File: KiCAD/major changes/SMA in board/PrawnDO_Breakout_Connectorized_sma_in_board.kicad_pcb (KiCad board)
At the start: 2 copper layers, 113 x 86.8 mm, 83 parts, among them IC1 74LVT245D,118, IC2 74LVT245D,118, IC3 74LVT245D,118, IC4 74LVT245D,118, J1 do15, J10 do6, J11 do5, J12 do4, J13 do3, J14 do2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

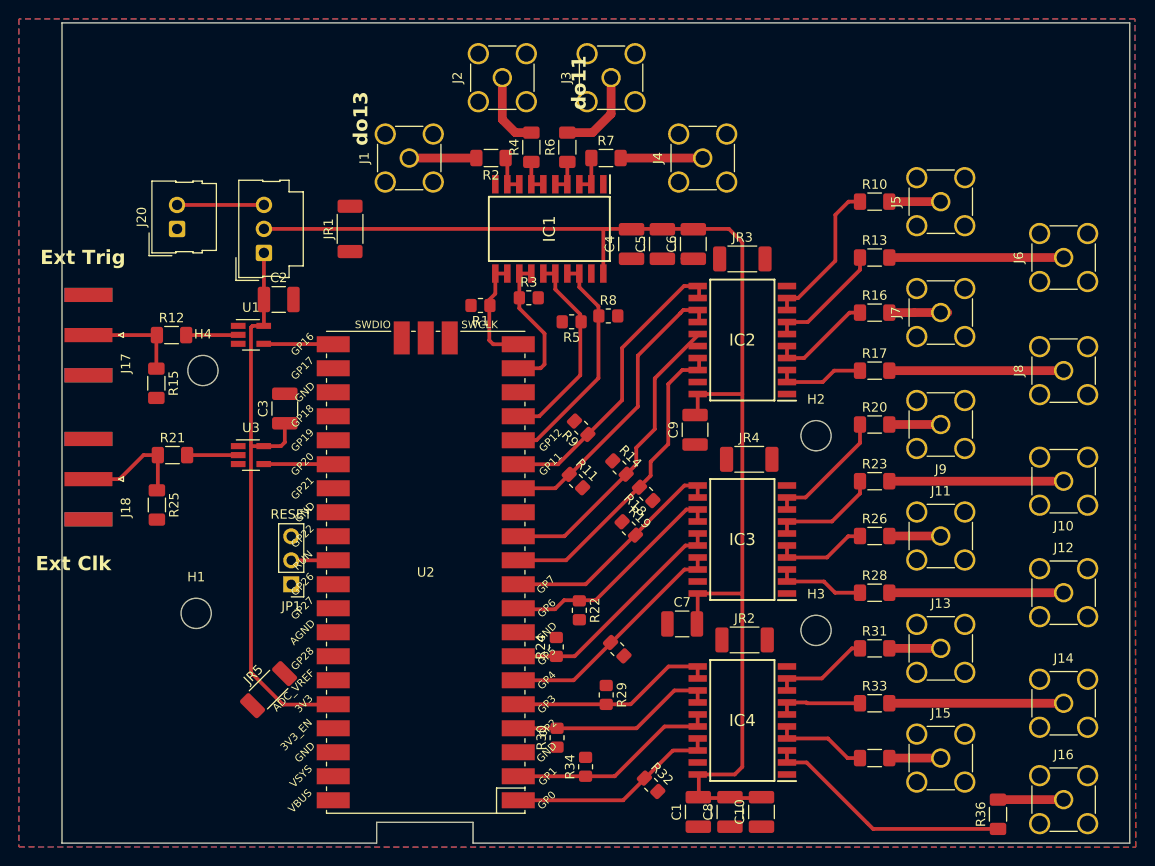
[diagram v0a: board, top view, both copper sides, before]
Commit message: Trace changes
Fixed some traces and added a connection to ground through pins on pico

Also made slot for USB slightly larger.

Moved resistor on bottom of board

Changed header footprint
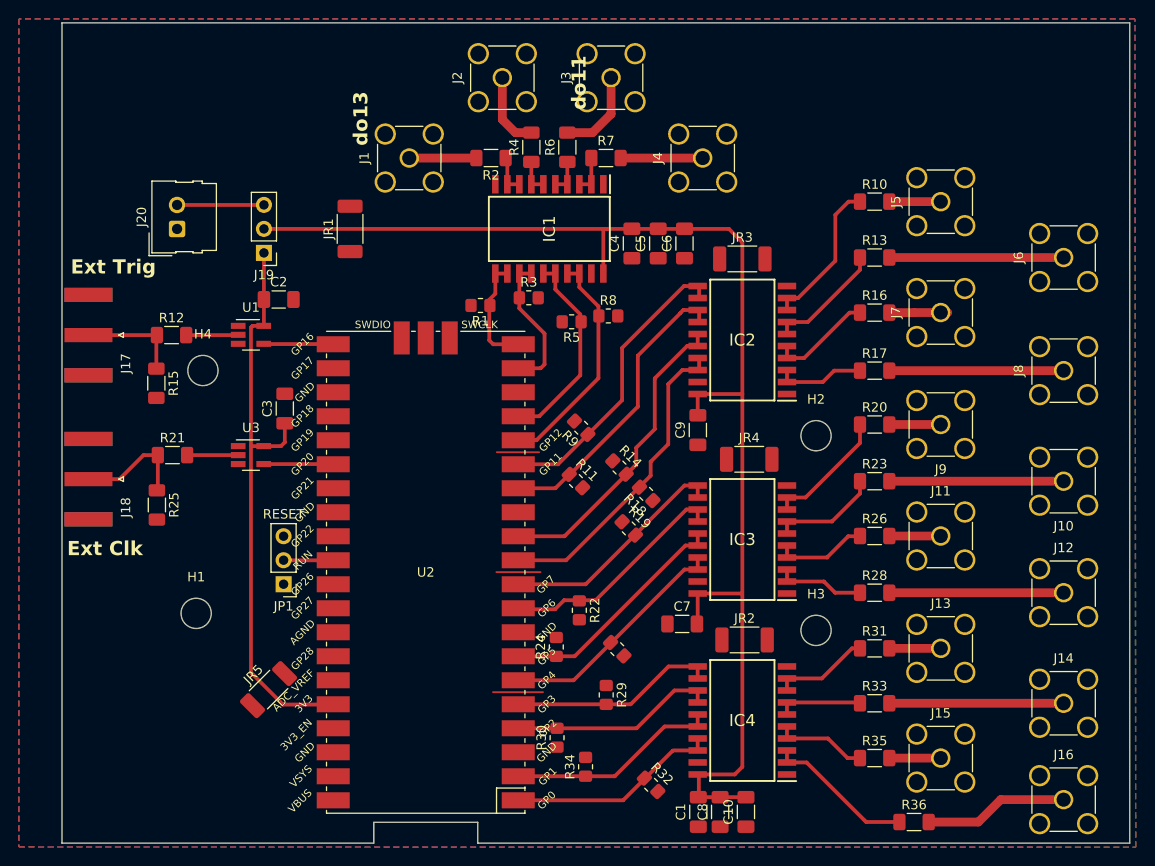
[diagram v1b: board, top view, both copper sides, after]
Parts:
- C1, C10, C2, C3, C4, C5, C6, C7, C8, C9: footprint Capacitor_SMD:C_1210_3225Metric_Pad1.33x2.70mm_HandSolder -> Capacitor_SMD:C_1206_3216Metric_Pad1.33x1.80mm_HandSolder
- J19: value Conn_01x03 -> PWR SEL; footprint Connector_Molex:Molex_SL_171971-0003_1x03_P2.54mm_Vertical -> Connector_PinHeader_2.54mm:PinHeader_1x03_P2.54mm_Vertical
- J20: value Conn_01x02 -> EXT PWR
- moved R36 8.92 mm to (162.1, 138.8), turned to 0 degrees
- moved C10 1.64 mm to (144.3, 137.7)
- moved C8 1.04 mm to (141.5, 137.7)
- moved C6 0.94 mm to (137.8, 77.5)
- moved JP1 0.81 mm to (95.3, 113.6)
- moved C5 0.44 mm to (135.0, 77.5)
- moved C9 0.30 mm to (139.2, 97.3)
- moved C4 0.07 mm to (132.2, 77.5)
- turned J19 to 180 degrees
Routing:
- net GND: track 0.00 -> 14.4 mm
- net Net-(IC4A-A0): track 26.5 -> 15.8 mm
- net do0: track 6.94 -> 15.3 mm
- net Power  Supply: track 140.3 -> 138.8 mm
- net Net-(JP1-C): track 5.36 -> 6.17 mm
- net Net-(IC2A-B2): track 33.1 -> 33.7 mm
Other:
- outline, holes or cut-outs redrawn

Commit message: Moved around mounting holes
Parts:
- moved H4 3.49 mm to (86.7, 94.5)
- moved H1 3.22 mm to (86.7, 113.5)
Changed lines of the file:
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@@
   )
   (footprint "MountingHole:MountingHole_3.2mm_M3_ISO7380" (layer "F.Cu")
-    (at 86.817 90.986)
+    (at 86.699896 94.475)
     (descr "Mounting Hole 3.2mm, no annular, M3, ISO7380")
     (tags "mounting hole 3.2mm no annular m3 iso7380")
@@
     (property "ki_keywords" "R res resistor")
     (attr smd)
-    (fp_text reference "R25" (at 0 -1.82 -90) (layer "F.SilkS")
+    (fp_text reference "R25" (at 0 -1.82 90) (layer "F.SilkS")
         (effects (font (size 1 1) (thickness 0.15)))
     )
-    (fp_text value "47k" (at 0 1.82 -90) (layer "F.Fab")
+    (fp_text value "47k" (at 0 1.82 90) (layer "F.Fab")
         (effects (font (size 1 1) (thickness 0.15)))
     )
-    (fp_text user "${REFERENCE}" (at 0 0 -90) (layer "F.Fab")
+    (fp_text user "${REFERENCE}" (at 0 0 90) (layer "F.Fab")
         (effects (font (size 0.8 0.8) (thickness 0.12)))
     )
@@
         (effects (font (size 1 1) (thickness 0.15)))
     )
-    (fp_text value "EXT PWR" (at 6.217 0.876 180) (layer "F.Fab")
+    (fp_text value "EXT PWR" (at 6.217 0.876) (layer "F.Fab")
         (effects (font (size 1 1) (thickness 0.15)))
     )
@@
         (effects (font (size 1 1) (thickness 0.15)))
     )
-    (fp_text user "GP0" (at -12.8 -24.13 225) (layer "F.SilkS")
+    (fp_text user "GP0" (at -12.8 -24.13 45) (layer "F.SilkS")
         (effects (font (size 0.8 0.8) (thickness 0.15)))
     )
@@
         (effects (font (size 0.8 0.8) (thickness 0.15)))
     )
-    (fp_text user "GP5" (at -12.8 -8.89 225) (layer "F.SilkS")
+    (fp_text user "GP5" (at -12.8 -8.89 45) (layer "F.SilkS")
         (effects (font (size 0.8 0.8) (thickness 0.15)))
     )
-    (fp_text user "GP1" (at -12.9 -21.6 225) (layer "F.SilkS")
+    (fp_text user "GP1" (at -12.9 -21.6 45) (layer "F.SilkS")
         (effects (font (size 0.8 0.8) (thickness 0.15)))
     )
@@
         (effects (font (size 0.8 0.8) (thickness 0.15)))
     )
-    (fp_text user "GP3" (at -12.8 -13.97 225) (layer "F.SilkS")
+    (fp_text user "GP3" (at -12.8 -13.97 45) (layer "F.SilkS")
         (effects (font (size 0.8 0.8) (thickness 0.15)))
     )
@@
         (effects (font (size 0.8 0.8) (thickness 0.15)))
     )
-    (fp_text user "GND" (at -12.8 -19.05 225) (layer "F.SilkS")
+    (fp_text user "GND" (at -12.8 -19.05 45) (layer "F.SilkS")
         (effects (font (size 0.8 0.8) (thickness 0.15)))
     )
@@
         (effects (font (size 0.8 0.8) (thickness 0.15)))
     )
-    (fp_text user "GP6" (at -12.8 -3.81 225) (layer "F.SilkS")
+    (fp_text user "GP6" (at -12.8 -3.81 45) (layer "F.SilkS")
         (effects (font (size 0.8 0.8) (thickness 0.15)))
     )
@@
         (effects (font (size 0.8 0.8) (thickness 0.15)))
     )
-    (fp_text user "GP7" (at -12.7 -1.3 225) (layer "F.SilkS")
+    (fp_text user "GP7" (at -12.7 -1.3 45) (layer "F.SilkS")
         (effects (font (size 0.8 0.8) (thickness 0.15)))
     )
@@
         (effects (font (size 0.8 0.8) (thickness 0.15)))
     )
-    (fp_text user "GP4" (at -12.8 -11.43 225) (layer "F.SilkS")
+    (fp_text user "GP4" (at -12.8 -11.43 45) (layer "F.SilkS")
         (effects (font (size 0.8 0.8) (thickness 0.15)))
     )
@@
         (effects (font (size 0.8 0.8) (thickness 0.15)))
     )
-    (fp_text user "GND" (at -12.8 -6.35 225) (layer "F.SilkS")
+    (fp_text user "GND" (at -12.8 -6.35 45) (layer "F.SilkS")
         (effects (font (size 0.8 0.8) (thickness 0.15)))
     )
-    (fp_text user "GP2" (at -12.9 -16.51 225) (layer "F.SilkS")
+    (fp_text user "GP2" (at -12.9 -16.51 45) (layer "F.SilkS")
         (effects (font (size 0.8 0.8) (thickness 0.15)))
     )
@@
     (property "ki_keywords" "R res resistor")
     (attr smd)
-    (fp_text reference "R15" (at 0 -1.82 -90) (layer "F.SilkS")
+    (fp_text reference "R15" (at 0 -1.82 90) (layer "F.SilkS")
         (effects (font (size 1 1) (thickness 0.15)))
     )
-    (fp_text value "47k" (at 0 1.82 -90) (layer "F.Fab")
+    (fp_text value "47k" (at 0 1.82 90) (layer "F.Fab")
         (effects (font (size 1 1) (thickness 0.15)))
     )
-    (fp_text user "${REFERENCE}" (at 0 0 -90) (layer "F.Fab")
+    (fp_text user "${REFERENCE}" (at 0 0 90) (layer "F.Fab")
         (effects (font (size 0.8 0.8) (thickness 0.12)))
     )
@@
   )
   (footprint "MountingHole:MountingHole_3.2mm_M3_ISO7380" (layer "F.Cu")
-    (at 86.1 116.686)
+    (at 86.699896 113.525)
     (descr "Mounting Hole 3.2mm, no annular, M3, ISO7380")
     (tags "mounting hole 3.2mm no annular m3 iso7380")
